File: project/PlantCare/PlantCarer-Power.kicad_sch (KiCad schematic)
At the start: 13 parts, among them SW1 SW_DPDT_x2, U1 AMS1117-3.3, U4 AMS1117-3.3, U5 AMS1117-3.3, U6 AMS1117-3.3

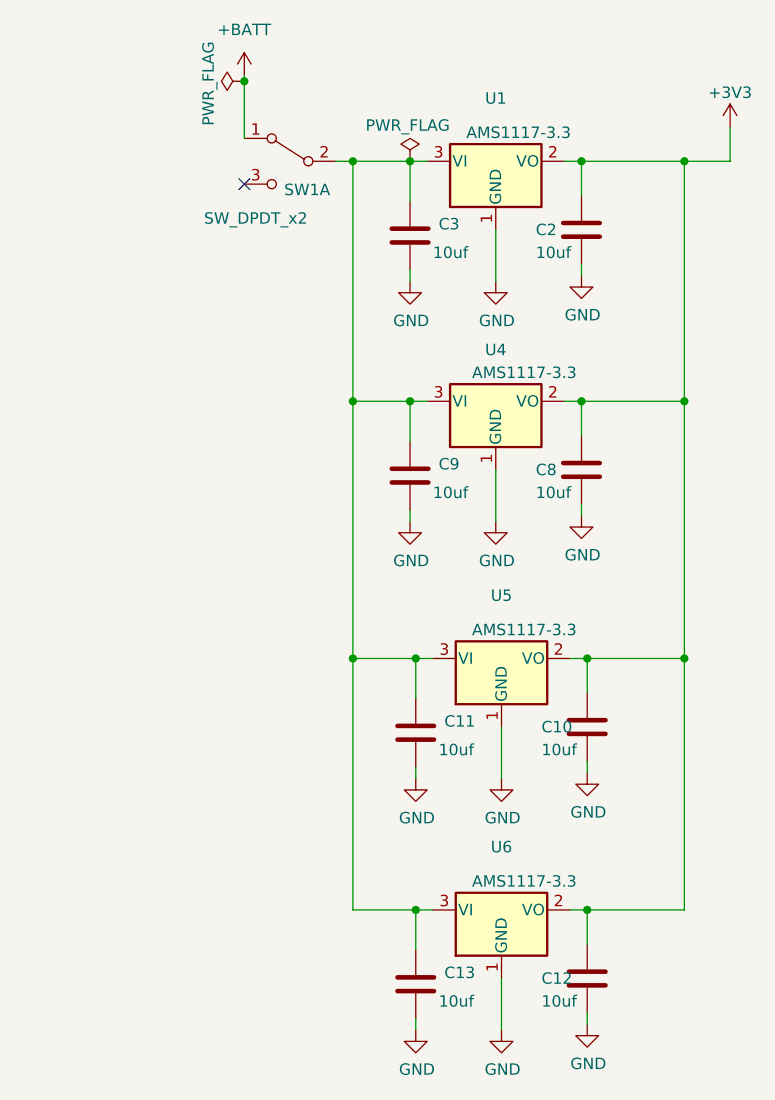
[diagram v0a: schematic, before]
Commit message: update plant carer 1.2
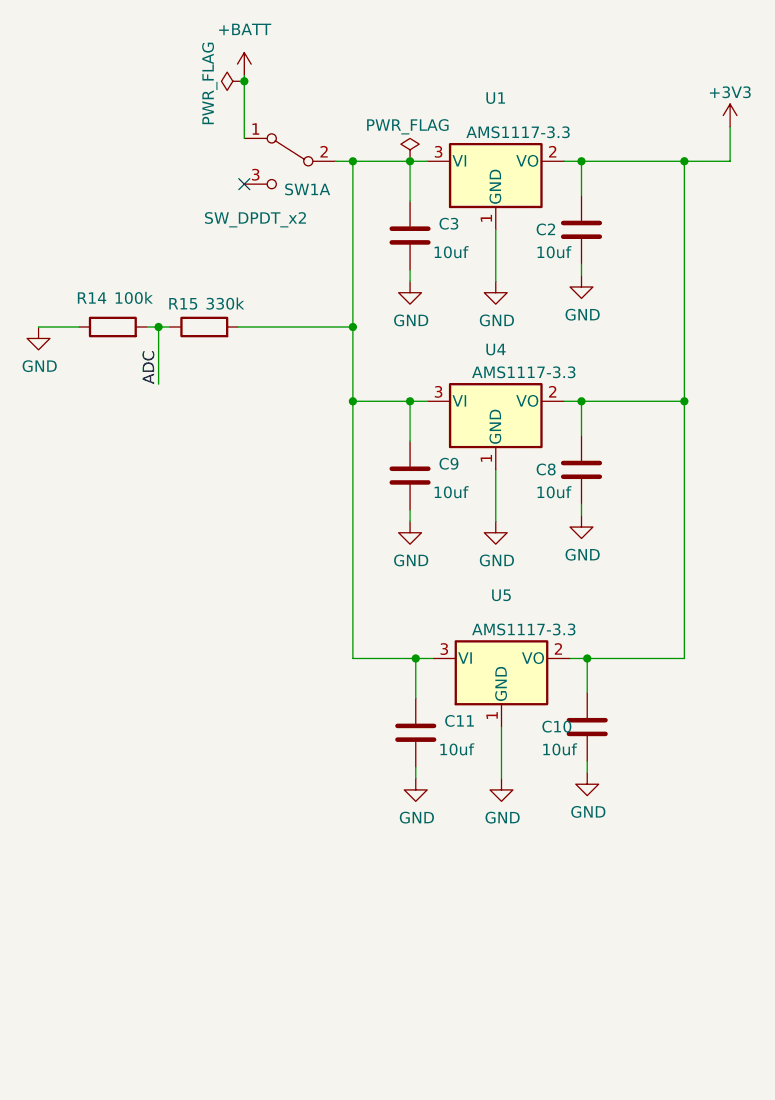
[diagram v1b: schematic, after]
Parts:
- removed C12, C13: 10uf, Capacitor_SMD:C_0402_1005Metric, symbol Device:C
- removed U6: AMS1117-3.3, Package_TO_SOT_SMD:SOT-223-3_TabPin2, symbol Regulator_Linear:AMS1117-3.3
- added R14: 100k, Resistor_SMD:R_0402_1005Metric, symbol Device:R
- added R15: 330k, Resistor_SMD:R_0402_1005Metric, symbol Device:R
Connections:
- net GND: now also R14.1
- net at C11.1, C3.1, C9.1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: now also R15.2
- new net ADC: R14.2, R15.1
